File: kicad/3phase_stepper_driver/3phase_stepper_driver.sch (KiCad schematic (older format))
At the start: 17 parts

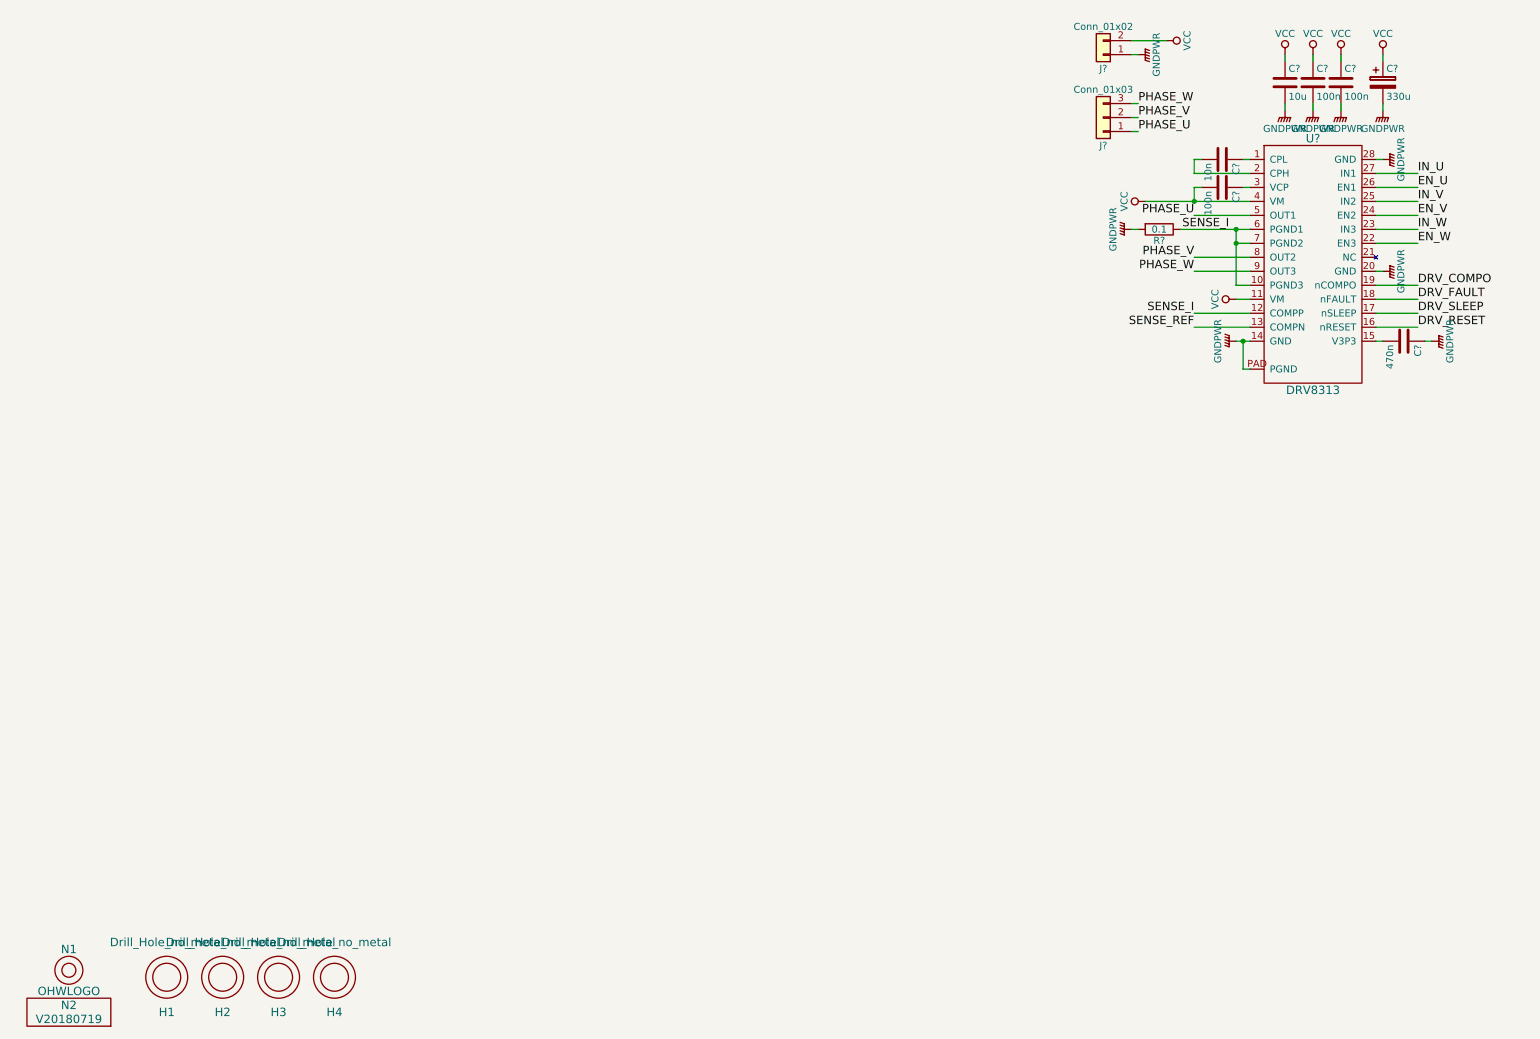
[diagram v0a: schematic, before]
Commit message: added LPC845, SWD programming, UART connection
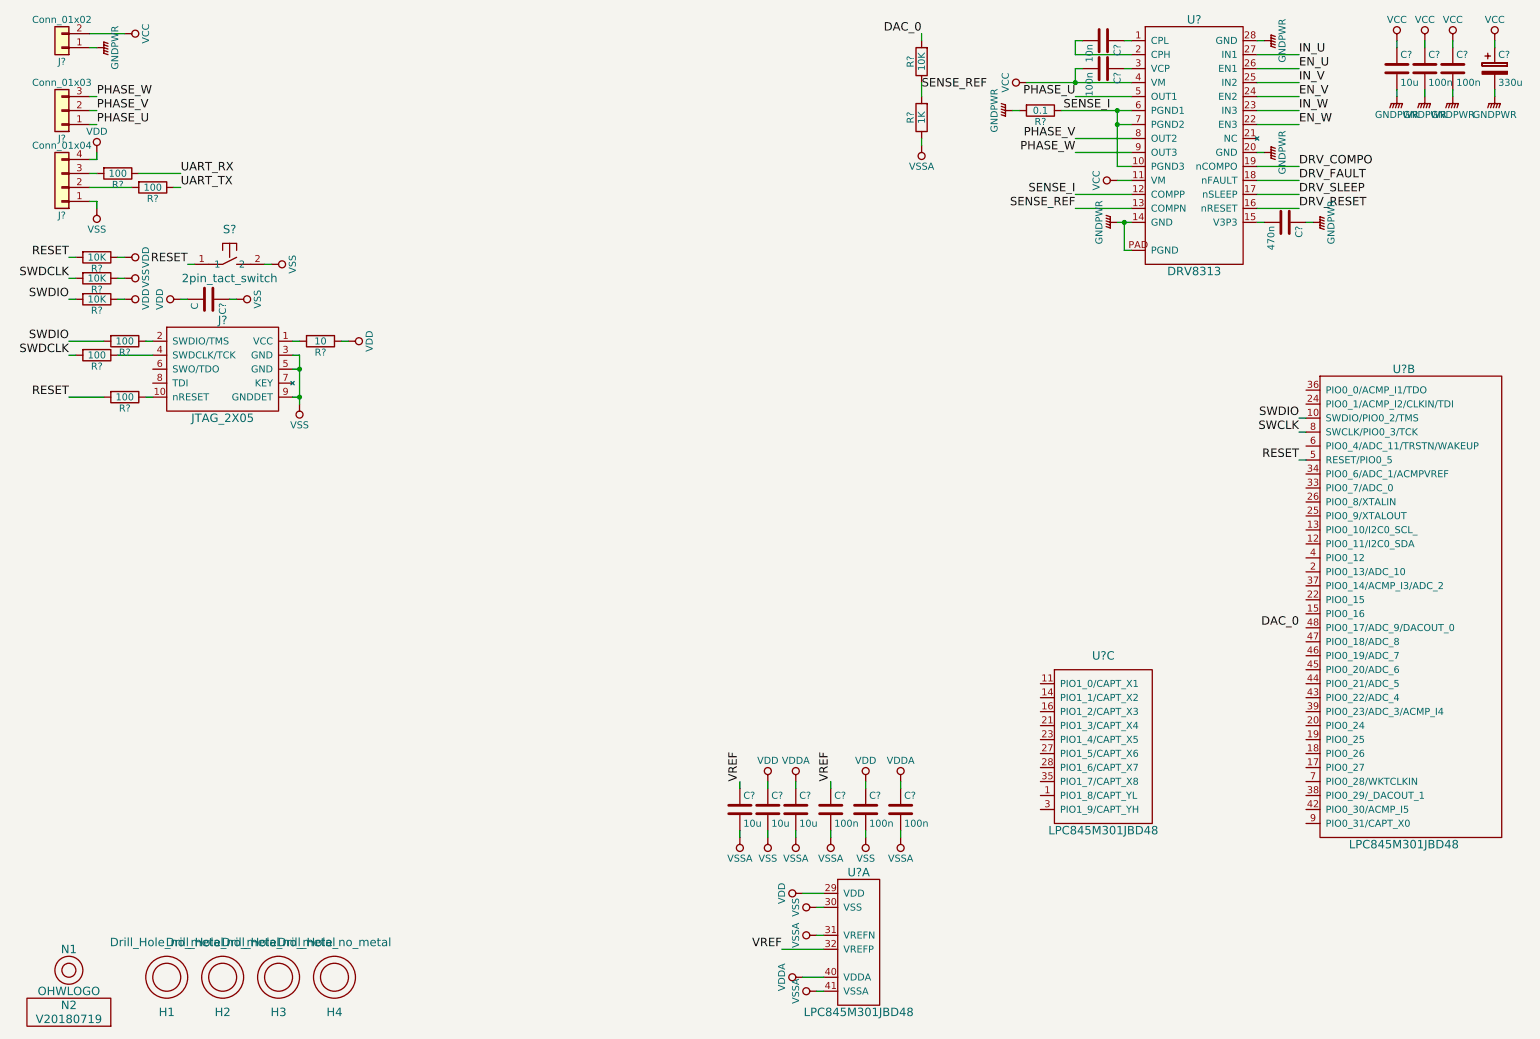
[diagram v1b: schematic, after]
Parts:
- added C?: C, symbol C
- added C? (x3): 100n, SquantorRcl:C_0603, symbol C
- added C? (x3): 10u, SquantorRcl:C_0805, symbol C
- added J?: JTAG_2X05, symbol JTAG_2X05
- added J?: Conn_01x04, symbol Conn_01x04
- added R? (x5): 100, SquantorRcl:R_0603, symbol R
- added R?: 10, SquantorRcl:R_0603, symbol R
- added R? (x4): 10K, SquantorRcl:R_0603, symbol R
- added R?: 1K, SquantorRcl:R_0603, symbol R
- added S?: 2pin_tact_switch, SquantorButtons:DTSM3, symbol 2pin_tact_switch
- added U? (x3): LPC845M301JBD48, symbol LPC845M301JBD48
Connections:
- net SENSE_REF: now also R?.1, R?.2
- new net: J?.1 (VCC), R?.2
- new net: J?.10 (nRESET), R?.1
- new net: J?.2 (SWDIO/TMS), R?.1
- new net: J?.4 (SWDCLK/TCK), R?.1
- new net: J?.2 (Pin_2), R?.2
- new net: J?.3 (Pin_3), R?.2
- new net DAC_0: R?.2
- new net RESET: R?.2, R?.2, S?.1, U?.5 (RESET/PIO0_5)
- new net SWCLK: U?.8 (SWCLK/PIO0_3/TCK)
- new net SWDCLK: R?.2, R?.2
- new net SWDIO: R?.2, R?.2, U?.10 (SWDIO/PIO0_2/TMS)
- new net UART_RX: R?.1
- new net UART_TX: R?.1
- new net VDD: C?.1, C?.1, C?.2, J?.4 (Pin_4), R?.1, R?.1, R?.1, U?.29 (VDD)
- new net VDDA: C?.1, C?.1, U?.40 (VDDA)
- new net VREF: C?.1, C?.1, U?.32 (VREFP)
- new net VSS: C?.1, C?.2, C?.2, J?.1 (Pin_1), J?.3 (GND), J?.5 (GND), J?.9 (GNDDET), R?.1, S?.2, U?.30 (VSS)
- new net VSSA: C?.2, C?.2, C?.2, C?.2, R?.1, U?.31 (VREFN), U?.41 (VSSA)
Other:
- moved on the sheet: C?, J?, R?, U?

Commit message: further updates
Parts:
- J4: renamed from J?; footprint (none) -> SquantorConnectors:Header-0127-2X05-H006
- R12: renamed from R?; footprint (none) -> SquantorRcl:R_1210
- U1: renamed from U?; footprint (none) -> SquantorIC:SOT313-2
- U2: renamed from U?; footprint (none) -> SquantorIC:HTSSOP-28_-TexasInstruments_PWP
- gave numbers to parts that had none: 29
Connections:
- no-connect marks 0 -> 2
